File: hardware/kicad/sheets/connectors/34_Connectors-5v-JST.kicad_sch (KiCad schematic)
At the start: 4 parts, among them U53 TPS22965DSGR

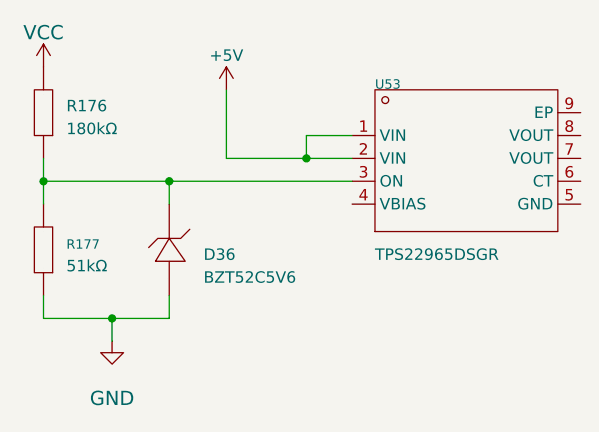
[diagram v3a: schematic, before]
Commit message: resheeted bms and fixed links for the 12v buck
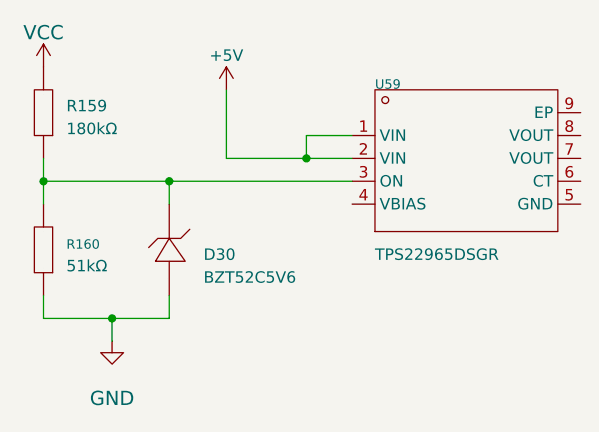
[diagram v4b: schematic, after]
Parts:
- renumbered D36 to D30, R176 to R159, R177 to R160, U53 to U59
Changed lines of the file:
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@@
 		(on_board yes)
 		(dnp no)
-		(property "Reference" "U53"
+		(property "Reference" "U59"
 			(at 149.86 64.77 0)
 			(effects
@@
 			(project "svea_powerboard_rev3"
 				(path "/3f85abf4-0b95-4c4a-b7e9-06f59ca1ea3d/5c2e021f-c2d4-49e2-8c36-9a64f1f12005/8d05c3b8-20a4-4a7f-9b20-01f8d5d5be51/9ed2a1cc-b4f2-4f0d-8c3f-2b2e0f2f5034"
-					(reference "U53")
+					(reference "U59")
 					(unit 1)
 				)
@@
 		(on_board yes)
 		(dnp no)
-		(property "Reference" "#PWR0264"
+		(property "Reference" "#PWR0164"
 			(at 133.35 64.77 0)
 			(effects
@@
 			(project "svea_powerboard_rev3"
 				(path "/3f85abf4-0b95-4c4a-b7e9-06f59ca1ea3d/5c2e021f-c2d4-49e2-8c36-9a64f1f12005/8d05c3b8-20a4-4a7f-9b20-01f8d5d5be51/9ed2a1cc-b4f2-4f0d-8c3f-2b2e0f2f5034"
-					(reference "#PWR0264")
+					(reference "#PWR0164")
 					(unit 1)
 				)
@@
 		(on_board yes)
 		(dnp no)
-		(property "Reference" "R177"
+		(property "Reference" "R160"
 			(at 115.57 82.55 90)
 			(effects
@@
 			(project "svea_powerboard_rev3"
 				(path "/3f85abf4-0b95-4c4a-b7e9-06f59ca1ea3d/5c2e021f-c2d4-49e2-8c36-9a64f1f12005/8d05c3b8-20a4-4a7f-9b20-01f8d5d5be51/9ed2a1cc-b4f2-4f0d-8c3f-2b2e0f2f5034"
-					(reference "R177")
+					(reference "R160")
 					(unit 1)
 				)
@@
 		(on_board yes)
 		(dnp no)
-		(property "Reference" "#PWR0263"
+		(property "Reference" "#PWR0163"
 			(at 120.65 92.71 0)
 			(effects
@@
 			(project "svea_powerboard_rev3"
 				(path "/3f85abf4-0b95-4c4a-b7e9-06f59ca1ea3d/5c2e021f-c2d4-49e2-8c36-9a64f1f12005/8d05c3b8-20a4-4a7f-9b20-01f8d5d5be51/9ed2a1cc-b4f2-4f0d-8c3f-2b2e0f2f5034"
-					(reference "#PWR0263")
+					(reference "#PWR0163")
 					(unit 1)
 				)
@@
 		(on_board yes)
 		(dnp no)
-		(property "Reference" "D36"
+		(property "Reference" "D30"
 			(at 130.81 83.82 90)
 			(effects
@@
 			(project "svea_powerboard_rev3"
 				(path "/3f85abf4-0b95-4c4a-b7e9-06f59ca1ea3d/5c2e021f-c2d4-49e2-8c36-9a64f1f12005/8d05c3b8-20a4-4a7f-9b20-01f8d5d5be51/9ed2a1cc-b4f2-4f0d-8c3f-2b2e0f2f5034"
-					(reference "D36")
+					(reference "D30")
 					(unit 1)
 				)
@@
 		(on_board yes)
 		(dnp no)
-		(property "Reference" "R176"
+		(property "Reference" "R159"
 			(at 115.57 67.31 90)
 			(effects
@@
 			(project "svea_powerboard_rev3"
 				(path "/3f85abf4-0b95-4c4a-b7e9-06f59ca1ea3d/5c2e021f-c2d4-49e2-8c36-9a64f1f12005/8d05c3b8-20a4-4a7f-9b20-01f8d5d5be51/9ed2a1cc-b4f2-4f0d-8c3f-2b2e0f2f5034"
-					(reference "R176")
+					(reference "R159")
 					(unit 1)
 				)
@@
 		(on_board yes)
 		(dnp no)
-		(property "Reference" "#PWR0265"
+		(property "Reference" "#PWR0162"
 			(at 113.03 62.23 0)
 			(effects
@@
 			(project "svea_powerboard_rev3"
 				(path "/3f85abf4-0b95-4c4a-b7e9-06f59ca1ea3d/5c2e021f-c2d4-49e2-8c36-9a64f1f12005/8d05c3b8-20a4-4a7f-9b20-01f8d5d5be51/9ed2a1cc-b4f2-4f0d-8c3f-2b2e0f2f5034"
-					(reference "#PWR0265")
-					(unit 1)
-				)
+					(reference "#PWR0162")
+					(unit 1)
+				)

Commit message: various improvements
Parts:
- renumbered D30 to D29, R159 to R148, R160 to R149, U59 to U58
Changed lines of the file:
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@@
 		(on_board yes)
 		(dnp no)
-		(property "Reference" "U59"
+		(property "Reference" "U58"
 			(at 149.86 64.77 0)
 			(effects
@@
 			(project "svea_powerboard_rev3"
 				(path "/3f85abf4-0b95-4c4a-b7e9-06f59ca1ea3d/5c2e021f-c2d4-49e2-8c36-9a64f1f12005/8d05c3b8-20a4-4a7f-9b20-01f8d5d5be51/9ed2a1cc-b4f2-4f0d-8c3f-2b2e0f2f5034"
-					(reference "U59")
+					(reference "U58")
 					(unit 1)
 				)
@@
 		(on_board yes)
 		(dnp no)
-		(property "Reference" "#PWR0164"
+		(property "Reference" "#PWR0175"
 			(at 133.35 64.77 0)
 			(effects
@@
 			(project "svea_powerboard_rev3"
 				(path "/3f85abf4-0b95-4c4a-b7e9-06f59ca1ea3d/5c2e021f-c2d4-49e2-8c36-9a64f1f12005/8d05c3b8-20a4-4a7f-9b20-01f8d5d5be51/9ed2a1cc-b4f2-4f0d-8c3f-2b2e0f2f5034"
-					(reference "#PWR0164")
+					(reference "#PWR0175")
 					(unit 1)
 				)
@@
 		(on_board yes)
 		(dnp no)
-		(property "Reference" "R160"
+		(property "Reference" "R149"
 			(at 115.57 82.55 90)
 			(effects
@@
 			(project "svea_powerboard_rev3"
 				(path "/3f85abf4-0b95-4c4a-b7e9-06f59ca1ea3d/5c2e021f-c2d4-49e2-8c36-9a64f1f12005/8d05c3b8-20a4-4a7f-9b20-01f8d5d5be51/9ed2a1cc-b4f2-4f0d-8c3f-2b2e0f2f5034"
-					(reference "R160")
+					(reference "R149")
 					(unit 1)
 				)
@@
 		(on_board yes)
 		(dnp no)
-		(property "Reference" "#PWR0163"
+		(property "Reference" "#PWR0174"
 			(at 120.65 92.71 0)
 			(effects
@@
 			(project "svea_powerboard_rev3"
 				(path "/3f85abf4-0b95-4c4a-b7e9-06f59ca1ea3d/5c2e021f-c2d4-49e2-8c36-9a64f1f12005/8d05c3b8-20a4-4a7f-9b20-01f8d5d5be51/9ed2a1cc-b4f2-4f0d-8c3f-2b2e0f2f5034"
-					(reference "#PWR0163")
+					(reference "#PWR0174")
 					(unit 1)
 				)
@@
 		(on_board yes)
 		(dnp no)
-		(property "Reference" "D30"
+		(property "Reference" "D29"
 			(at 130.81 83.82 90)
 			(effects
@@
 			(project "svea_powerboard_rev3"
 				(path "/3f85abf4-0b95-4c4a-b7e9-06f59ca1ea3d/5c2e021f-c2d4-49e2-8c36-9a64f1f12005/8d05c3b8-20a4-4a7f-9b20-01f8d5d5be51/9ed2a1cc-b4f2-4f0d-8c3f-2b2e0f2f5034"
-					(reference "D30")
+					(reference "D29")
 					(unit 1)
 				)
@@
 		(on_board yes)
 		(dnp no)
-		(property "Reference" "R159"
+		(property "Reference" "R148"
 			(at 115.57 67.31 90)
 			(effects
@@
 			(project "svea_powerboard_rev3"
 				(path "/3f85abf4-0b95-4c4a-b7e9-06f59ca1ea3d/5c2e021f-c2d4-49e2-8c36-9a64f1f12005/8d05c3b8-20a4-4a7f-9b20-01f8d5d5be51/9ed2a1cc-b4f2-4f0d-8c3f-2b2e0f2f5034"
-					(reference "R159")
+					(reference "R148")
 					(unit 1)
 				)
@@
 		(on_board yes)
 		(dnp no)
-		(property "Reference" "#PWR0162"
+		(property "Reference" "#PWR0173"
 			(at 113.03 62.23 0)
 			(effects
@@
 			(project "svea_powerboard_rev3"
 				(path "/3f85abf4-0b95-4c4a-b7e9-06f59ca1ea3d/5c2e021f-c2d4-49e2-8c36-9a64f1f12005/8d05c3b8-20a4-4a7f-9b20-01f8d5d5be51/9ed2a1cc-b4f2-4f0d-8c3f-2b2e0f2f5034"
-					(reference "#PWR0162")
-					(unit 1)
-				)
+					(reference "#PWR0173")
+					(unit 1)
+				)

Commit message: various improvements
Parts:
- removed D29: BZT52C5V6, Diode_SMD:SOD-123, symbol 5v rail sm-easyedapro:BZT52C5V6_C173406
- removed R148: 180kΩ, Resistor_SMD:R_0603_1608Metric, symbol 5v rail sm-easyedapro:0603WAF1803T5E
- removed R149: 51kΩ, Resistor_SMD:R_0603_1608Metric, symbol 5v rail sm-easyedapro:0603WAF5102T5E
- removed U58: TPS22965DSGR, 5v rail sm-easyedapro:UDFN-8_L2.0-W2.0-P0.50-TL-EP, symbol 5v rail sm-easyedapro:TPS22965DSGR
